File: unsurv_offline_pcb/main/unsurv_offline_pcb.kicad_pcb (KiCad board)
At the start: 4 copper layers, 35 x 50 mm, 59 parts, among them J1 10103594-0001LF, J2 S2B-PH-SM4-TB_LF__SN_, J3 1.27mm_female_connector, Q1 Q_PMOS_GSD, Q2 UMH3N, U1 MCP73831-2-OT, U2 APX803L20, U3 NCP59800, U4 MPU-6050_NRND, U5 ESP32-WROOM-32, U6 ublox_SAM-M8Q, U7 CH340G

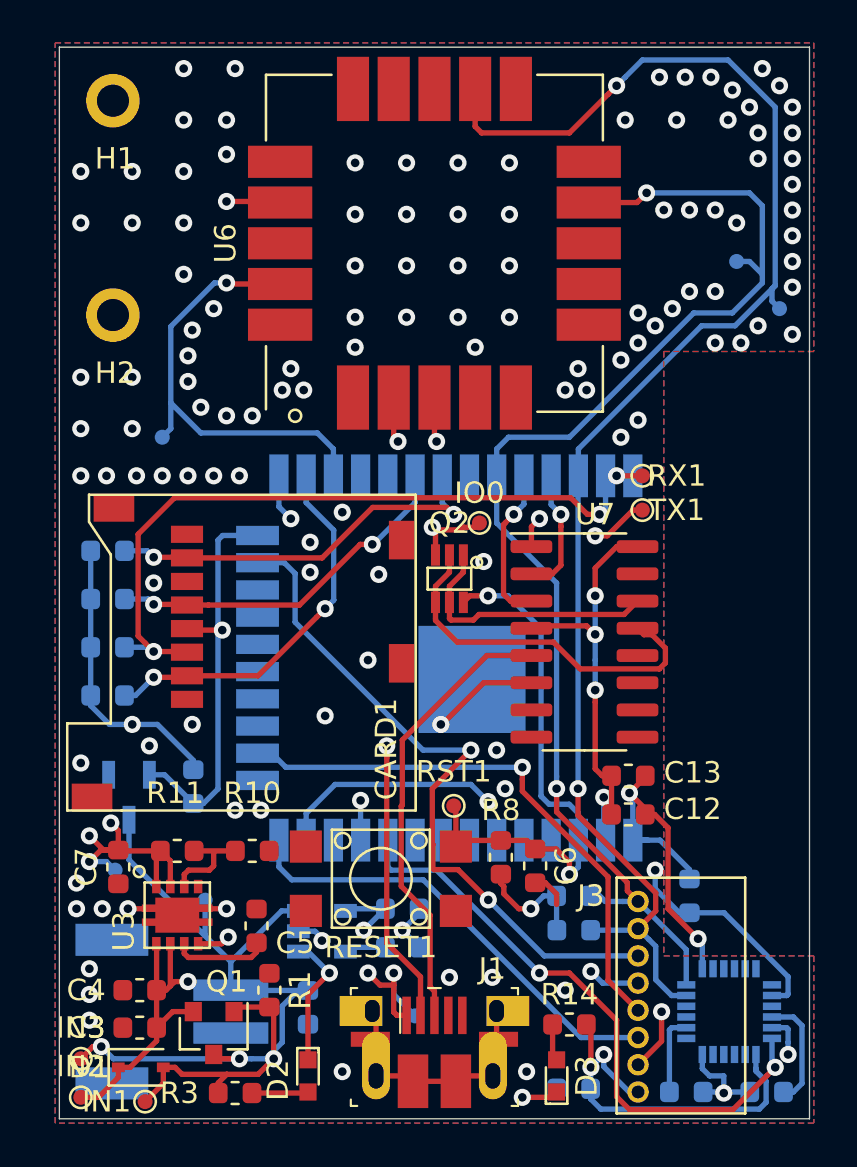
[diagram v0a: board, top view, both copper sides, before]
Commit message: added battery monitoring circuit
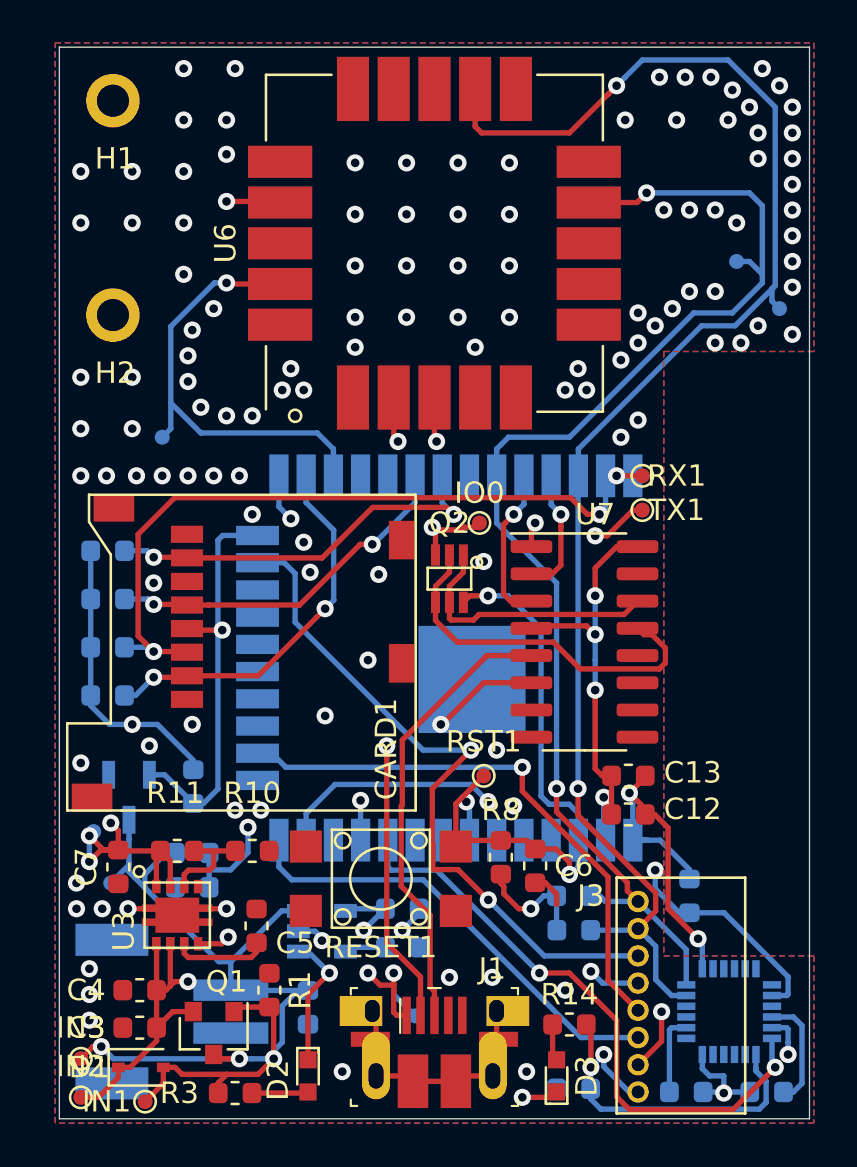
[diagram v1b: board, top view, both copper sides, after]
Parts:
- added R15: 100k, Resistor_SMD:R_0603_1608Metric, B.Cu at (81.2, 112.6)
- added R16: 100k, Resistor_SMD:R_0603_1608Metric, B.Cu at (81.2, 114.2)
- moved BAT1 4.47 mm to (77.4, 114.0)
- moved 3V3 2.06 mm to (76.6, 111.6)
- moved RST1 1.98 mm to (94.8, 109.0)
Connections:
- U5 pad 7: Net-(U5-Pad7) -> 35
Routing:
- net 35: track 0.00 -> 17.5 mm, vias 0 -> 2
- net +BATT: track 34.2 -> 36.7 mm
- net RESET: track 25.7 -> 27.6 mm
- net GND: track 39.4 -> 40.6 mm

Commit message: fixed microvias
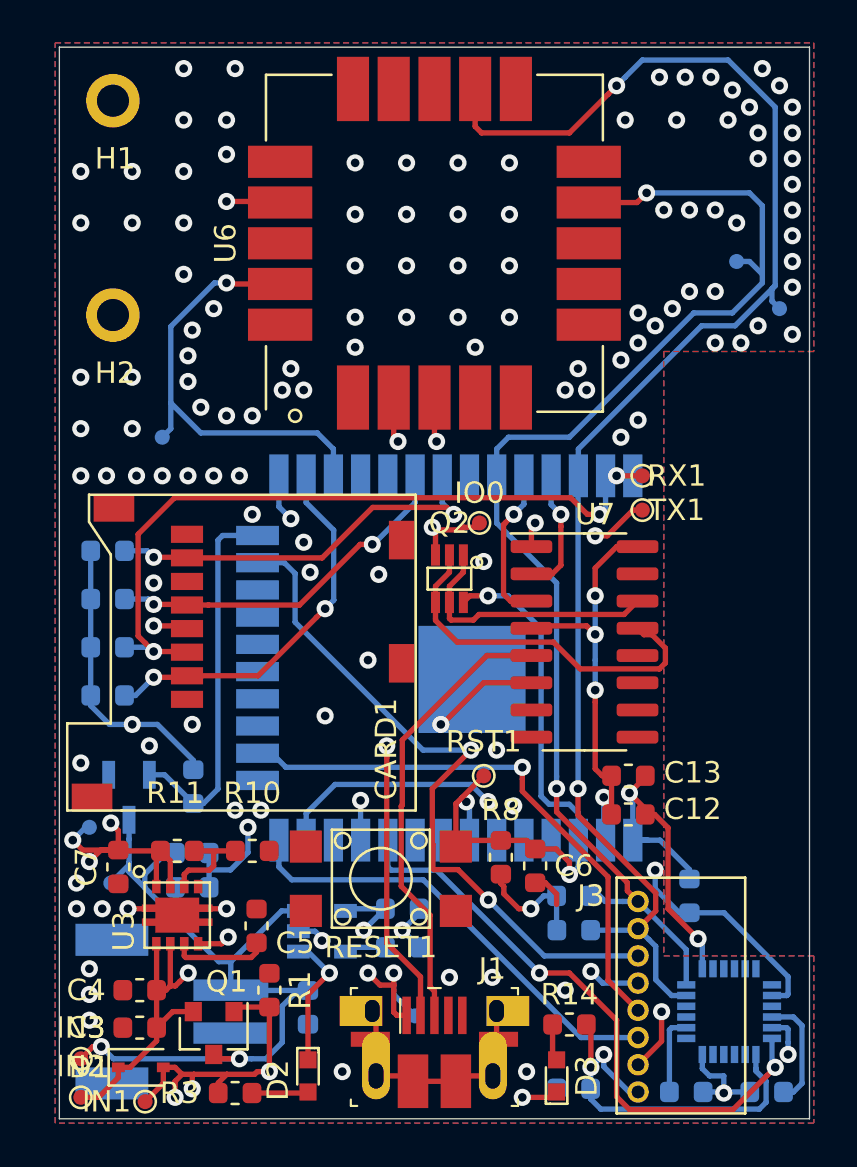
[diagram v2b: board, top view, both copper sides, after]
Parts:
- U6: footprint RF_GPS:ublox_SAM-M8Q_HandSolder -> unsurv_offline_pcb_footprints:ublox_SAM-M8Q_HandSolder
- moved 3V3 0.28 mm to (76.4, 111.4)
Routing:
- net +5V: track 22.7 -> 24.6 mm, vias 4 -> 6
- net 35: track 17.5 -> 18.1 mm

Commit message: added pps LED + fixed F.Mask
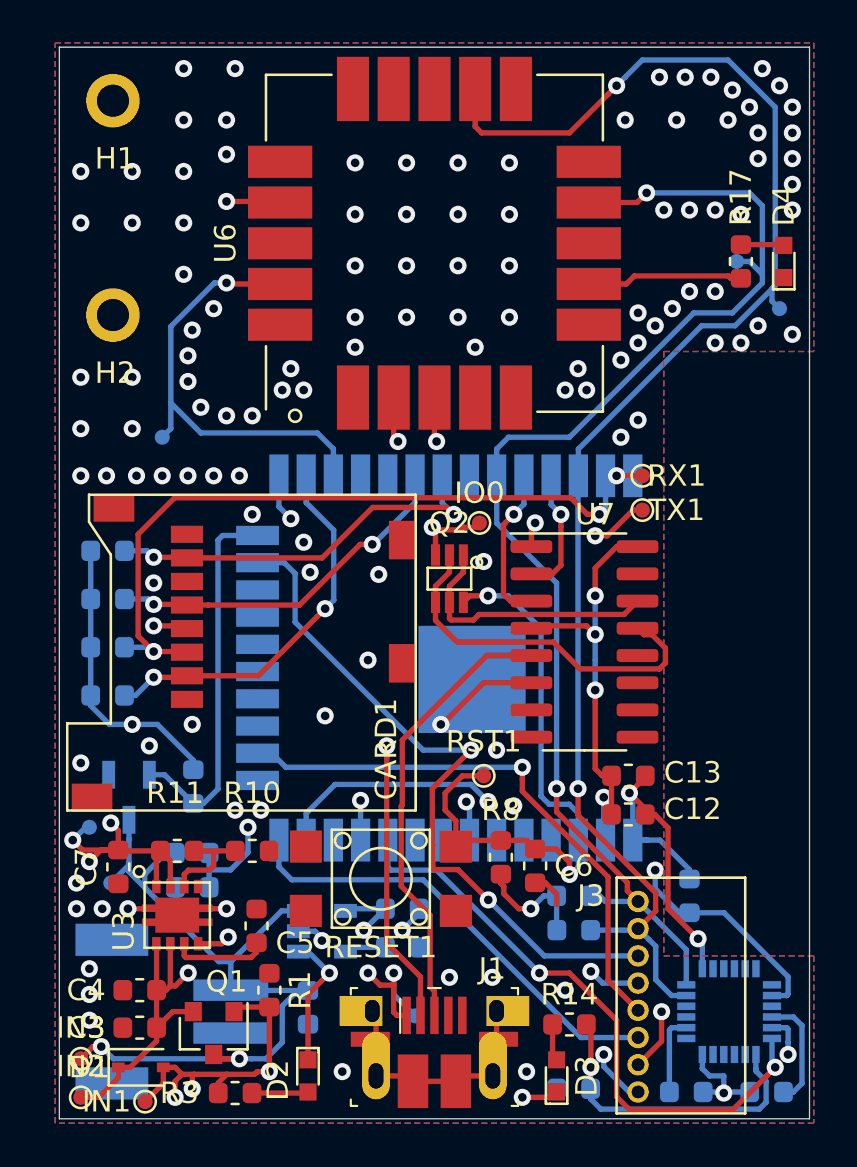
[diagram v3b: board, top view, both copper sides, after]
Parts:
- added D4: LED, digikey-footprints:LED_0603, F.Cu at (108.8, 85.0)
- added R17: 1k, Resistor_SMD:R_0603_1608Metric, F.Cu at (106.8, 85.0)
- H1, H2: footprint MountingHole:MountingHole_2.2mm_M2_Pad -> unsurv_offline_pcb_footprints:MountingHole_1.5mm_hole_in_FPaste
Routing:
- net Net-(R17-Pad1): track 0.00 -> 7.30 mm
- net Net-(D4-Pad2): track 0.00 -> 2.02 mm
- net RESET: track 27.6 -> 28.6 mm
- net GND: vias 127 -> 124

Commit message: 3.5 cm x 5 cm prototype
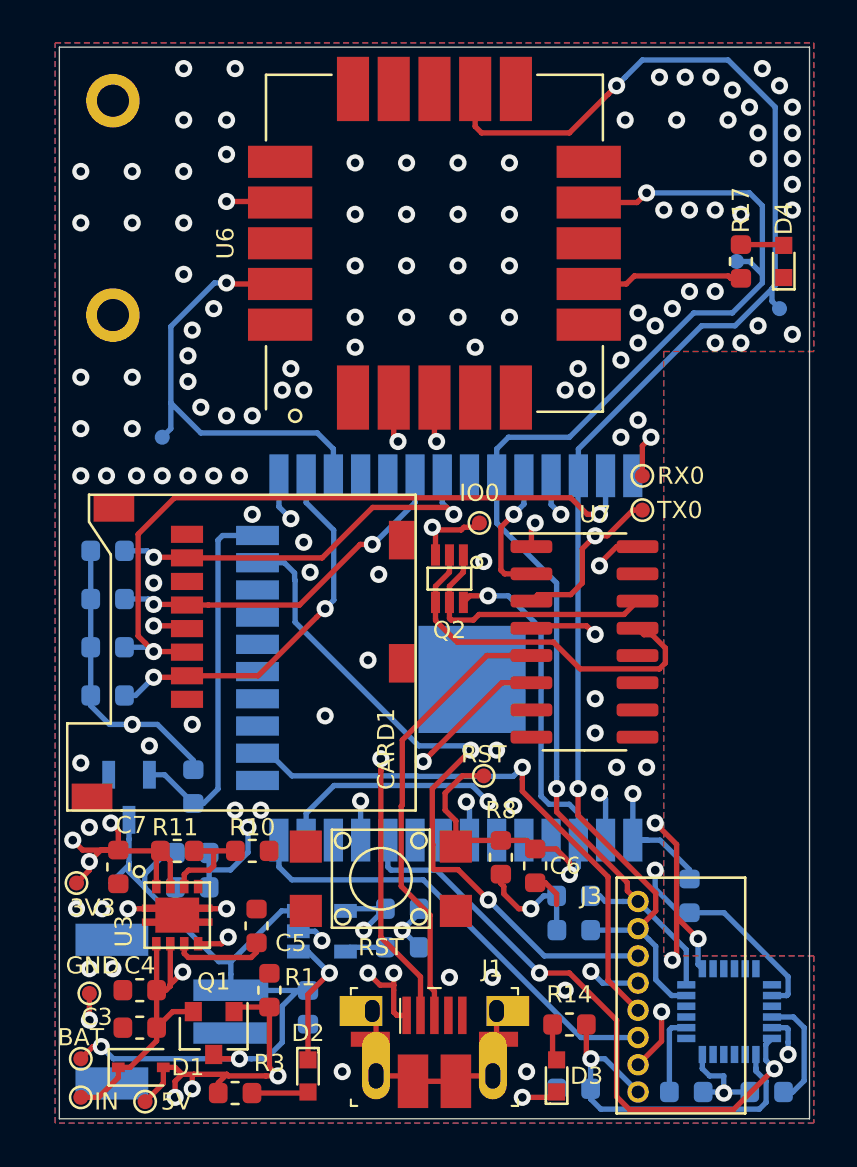
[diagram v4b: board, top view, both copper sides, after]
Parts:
- removed 5V1, BAT1: TestPoint, unsurv_offline_pcb_footprints:TestPoint_Pad_D0.7mm
- removed C12: 100nF, Capacitor_SMD:C_0603_1608Metric
- removed C13: 10yF, Capacitor_SMD:C_0603_1608Metric
- added GND: TestPoint, unsurv_offline_pcb_footprints:TestPoint_Pad_D0.7mm, F.Cu at (76.4, 119.2)
- 3V3: moved to F.Cu
- moved 3V3 2.67 mm to (75.8, 114.0)
- renumbered IN1 to 5V, IN3 to BAT, GINT1 to GINT, IN2 to IN, RST1 to RST, RESET1 to RST, RX1 to RX0, SCL1 to SCL, SDA1 to SDA, TX1 to TX0
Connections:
- U7 pad 2: TX0 -> RX0
- U7 pad 3: RX0 -> TX0
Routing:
- net +3V3: track 87.6 -> 75.2 mm, vias 16 -> 14
- net RX0: track 14.1 -> 16.2 mm
- net +5V: track 24.6 -> 23.0 mm
- net TX0: track 10.8 -> 12.1 mm
- net GND: track 40.6 -> 40.9 mm, vias 124 -> 130
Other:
- net class Default: clearance 0.2 -> 0.1; via_dia 0.8 -> 0.4; via_drill 0.4 -> 0.3
- rule trace_clearance: 0.2 -> 0.1

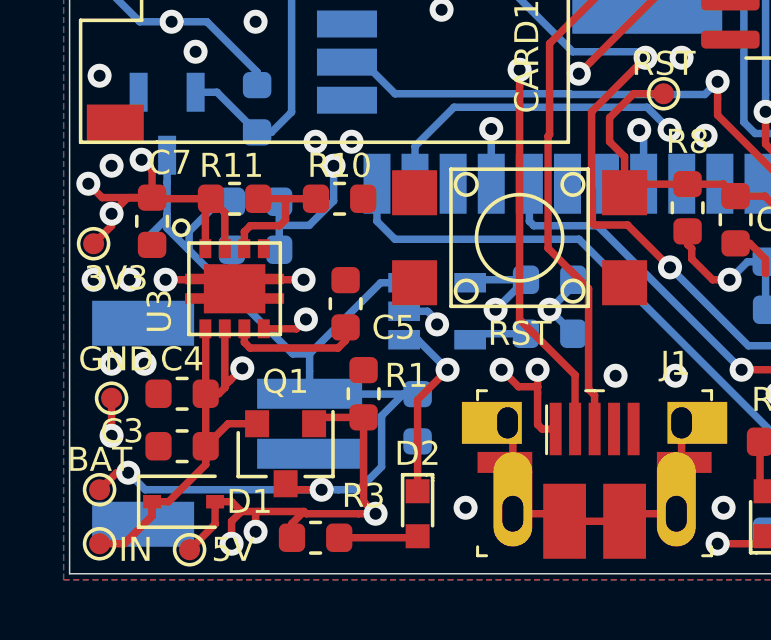
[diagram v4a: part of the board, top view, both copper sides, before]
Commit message: no conn to pin 12, defines memory voltage at boot
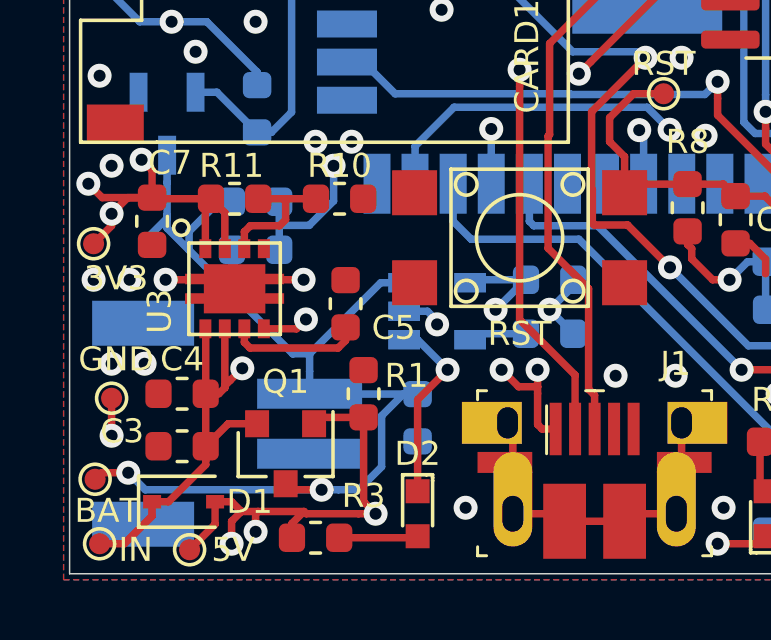
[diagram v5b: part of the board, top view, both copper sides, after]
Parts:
- moved BAT 0.38 mm to (75.8, 121.8)
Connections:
- J3 pad 3: 12 -> 27
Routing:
- net 12: track 21.3 -> 0.00 mm
- net 27: track 0.00 -> 18.8 mm
- net 35: track 18.1 -> 19.8 mm
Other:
- net class Default: via_dia 0.4 -> 0.6
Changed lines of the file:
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@@
     (thickness 1.6)
     (drawings 5)
-    (tracks 752)
+    (tracks 754)
     (zones 0)
     (modules 60)
@@
   (page A4)
   (layers
-    (0 F.Cu signal)
-    (1 GND power)
-    (2 PWR power)
-    (31 B.Cu signal)
+    (0 F.Cu signal hide)
+    (1 GND power hide)
+    (2 PWR power hide)
+    (31 B.Cu signal hide)
     (32 B.Adhes user hide)
     (33 F.Adhes user hide)
@@
     (zone_45_only no)
     (trace_min 0.2)
-    (via_size 0.4)
+    (via_size 0.6)
     (via_drill 0.3)
     (via_min_size 0.4)
@@
     (clearance 0.1)
     (trace_width 0.25)
-    (via_dia 0.4)
+    (via_dia 0.6)
     (via_drill 0.3)
     (uvia_dia 0.3)
@@
     (tags capacitor)
     (attr smd)
-    (fp_text reference C10 (at -1.2 1.15) (layer B.SilkS)
+    (fp_text reference C10 (at -1.15 1.05) (layer B.SilkS)
       (effects (font (size 0.8 0.8) (thickness 0.1)) (justify mirror))
     )
@@
     (tags capacitor)
     (attr smd)
-    (fp_text reference C11 (at -1.45 -1.15) (layer B.SilkS)
+    (fp_text reference C11 (at -0.6 -1.15) (layer B.SilkS)
       (effects (font (size 0.8 0.8) (thickness 0.1)) (justify mirror))
     )
@@
       (net 1 GND))
     (pad 3 thru_hole circle (at -1.46 0 90) (size 1 1) (drill 0.6) (layers *.Cu *.Mask)
-      (net 19 12))
+      (net 76 27))
     (pad 4 thru_hole circle (at -0.19 0 90) (size 1 1) (drill 0.6) (layers *.Cu *.Mask)
       (net 20 13))
@@
   )
   (module unsurv_offline_pcb_footprints:TestPoint_Pad_D0.7mm (layer F.Cu)
-    (at 76 122.2)
+    (at 75.85 121.85)
     (descr "SMD pad as test Point, diameter 1.0mm")
     (tags "test point SMD pad")
     (attr virtual)
-    (fp_text reference BAT (at 0 -1) (layer F.SilkS)
+    (fp_text reference BAT (at 0.4 1.05) (layer F.SilkS)
       (effects (font (size 0.8 0.8) (thickness 0.1)))
     )
@@
   (segment (start 83.4 122.2) (end 77.522649 122.2) (width 0.25) (layer B.Cu) (net 3))
   (segment (start 77.522649 122.2) (end 76.954701 121.632052) (width 0.25) (layer B.Cu) (net 3))
-  (segment (start 76.567948 121.632052) (end 76 122.2) (width 0.25) (layer F.Cu) (net 3))
-  (segment (start 76.954701 121.632052) (end 76.567948 121.632052) (width 0.25) (layer F.Cu) (net 3))
   (segment (start 78.25 111.95) (end 78.25 111.05) (width 0.25) (layer B.Cu) (net 3))
   (segment (start 83 117.67) (end 82.438506 117.67) (width 0.25) (layer B.Cu) (net 3))
@@
   (segment (start 78.984253 114.215747) (end 78.984253 113.590747) (width 0.25) (layer B.Cu) (net 3))
   (segment (start 82.438506 117.67) (end 78.984253 114.215747) (width 0.25) (layer B.Cu) (net 3))
+  (segment (start 76.067948 121.632052) (end 75.85 121.85) (width 0.25) (layer F.Cu) (net 3))
+  (segment (start 76.954701 121.632052) (end 76.067948 121.632052) (width 0.25) (layer F.Cu) (net 3))
   (segment (start 80.825 117.285002) (end 81.014999 117.475001) (width 0.25) (layer F.Cu) (net 4))
   (segment (start 84.2 117.225) (end 84.2 116.7875) (width 0.25) (layer F.Cu) (net 4))
@@
   (segment (start 108.250001 86.276997) (end 108.250001 86.850001) (width 0.25) (layer B.Cu) (net 18))
   (segment (start 108.4 86.126998) (end 108.250001 86.276997) (width 0.25) (layer B.Cu) (net 18))
-  (segment (start 85.245 113.25) (end 85.245 112) (width 0.25) (layer B.Cu) (net 19))
-  (segment (start 91.977008 113.85001) (end 85.84501 113.85001) (width 0.25) (layer B.Cu) (net 19))
-  (segment (start 99.336998 121.21) (end 91.977008 113.85001) (width 0.25) (layer B.Cu) (net 19))
-  (segment (start 85.84501 113.85001) (end 85.245 113.25) (width 0.25) (layer B.Cu) (net 19))
-  (segment (start 102 121.21) (end 99.336998 121.21) (width 0.25) (layer B.Cu) (net 19))
+  (segment (start 99.336998 121.21) (end 91.977008 113.85001) (width 0.25) (layer B.Cu) (net 76))
+  (segment (start 102 121.21) (end 99.336998 121.21) (width 0.25) (layer B.Cu) (net 76))
   (via (at 96.6 108.6) (size 0.8) (drill 0.4) (layers F.Cu B.Cu) (net 20))
   (segment (start 96.6 109.165685) (end 96.6 108.6) (width 0.25) (layer F.Cu) (net 20))
@@
   (via (at 89.055 110.175021) (size 0.8) (drill 0.4) (layers F.Cu B.Cu) (net 75))
   (segment (start 89.454999 110.57502) (end 89.055 110.175021) (width 0.25) (layer PWR) (net 75))
+  (segment (start 87.785 113.25) (end 87.785 112) (width 0.25) (layer B.Cu) (net 76))
+  (segment (start 88.38501 113.85001) (end 87.785 113.25) (width 0.25) (layer B.Cu) (net 76))
+  (segment (start 91.977008 113.85001) (end 88.38501 113.85001) (width 0.25) (layer B.Cu) (net 76))
   (segment (start 103.575 120.75) (end 104.25 120.75) (width 0.25) (layer B.Cu) (net 77))
   (segment (start 103.564998 120.75) (end 103.575 120.75) (width 0.25) (layer B.Cu) (net 77))
@@
   (segment (start 83.8 112.575) (end 83.8 111.4) (width 0.25) (layer B.Cu) (net 82))
   (segment (start 82.9875 113.3875) (end 83.8 112.575) (width 0.25) (layer B.Cu) (net 82))
+  (segment (start 85.074999 111.325001) (end 83.874999 111.325001) (width 0.25) (layer PWR) (net 82))
+  (segment (start 89.05 107.35) (end 85.074999 111.325001) (width 0.25) (layer PWR) (net 82))
+  (segment (start 93.421662 110.212653) (end 92.359009 109.15) (width 0.25) (layer PWR) (net 82))
+  (segment (start 91.875026 109.15) (end 90.075026 107.35) (width 0.25) (layer PWR) (net 82))
   (segment (start 83.874999 111.325001) (end 83.8 111.4) (width 0.25) (layer PWR) (net 82))
-  (segment (start 93.421662 110.212653) (end 92.629008 109.419999) (width 0.25) (layer PWR) (net 82))
   (segment (start 93.987347 110.212653) (end 93.421662 110.212653) (width 0.25) (layer PWR) (net 82))
-  (segment (start 92.629008 109.419999) (end 86.653003 109.419999) (width 0.25) (layer PWR) (net 82))
-  (segment (start 86.653003 109.419999) (end 84.748001 111.325001) (width 0.25) (layer PWR) (net 82))
-  (segment (start 84.748001 111.325001) (end 83.874999 111.325001) (width 0.25) (layer PWR) (net 82))
+  (segment (start 92.359009 109.15) (end 91.875026 109.15) (width 0.25) (layer PWR) (net 82))
+  (segment (start 90.075026 107.35) (end 89.05 107.35) (width 0.25) (layer PWR) (net 82))
   (segment (start 108.7625 84.2125) (end 108.8 84.25) (width 0.25) (layer F.Cu) (net 83))
   (segment (start 106.8 84.2125) (end 108.7625 84.2125) (width 0.25) (layer F.Cu) (net 83))
